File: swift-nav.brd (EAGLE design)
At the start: 53 x 53 mm, 167 parts, among them J1 SMA_EDGE, J6 ZX62-B-5PA, U1 6SLX9FTG256, U10 MAX2769, U12 PT7M8206B33TA5EX, U13 M25PX80, U2 LTC3407A_DFN, U3 STM32-M-64-LQFP, U4 7Q-16.368MBG-T, U5 SMA_PATCH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

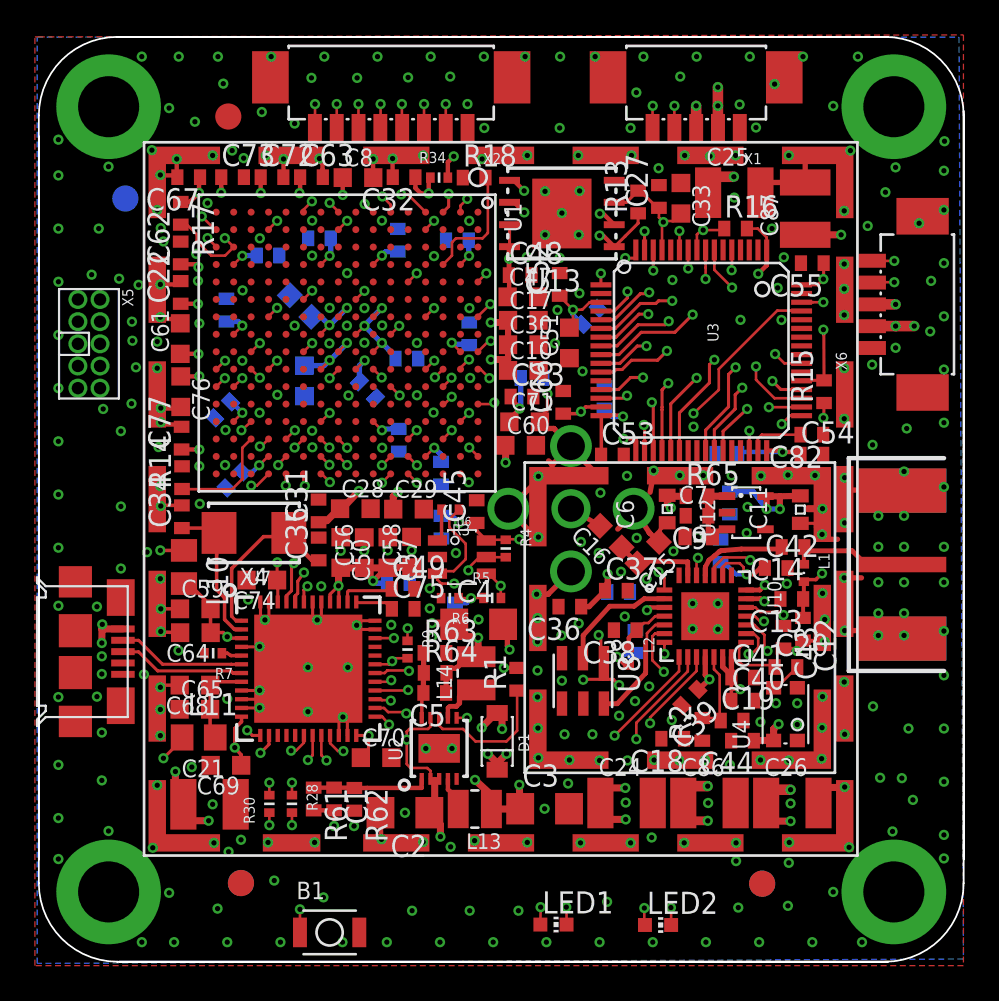
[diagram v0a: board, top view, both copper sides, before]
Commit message: Moved around a few vias and added a few more.
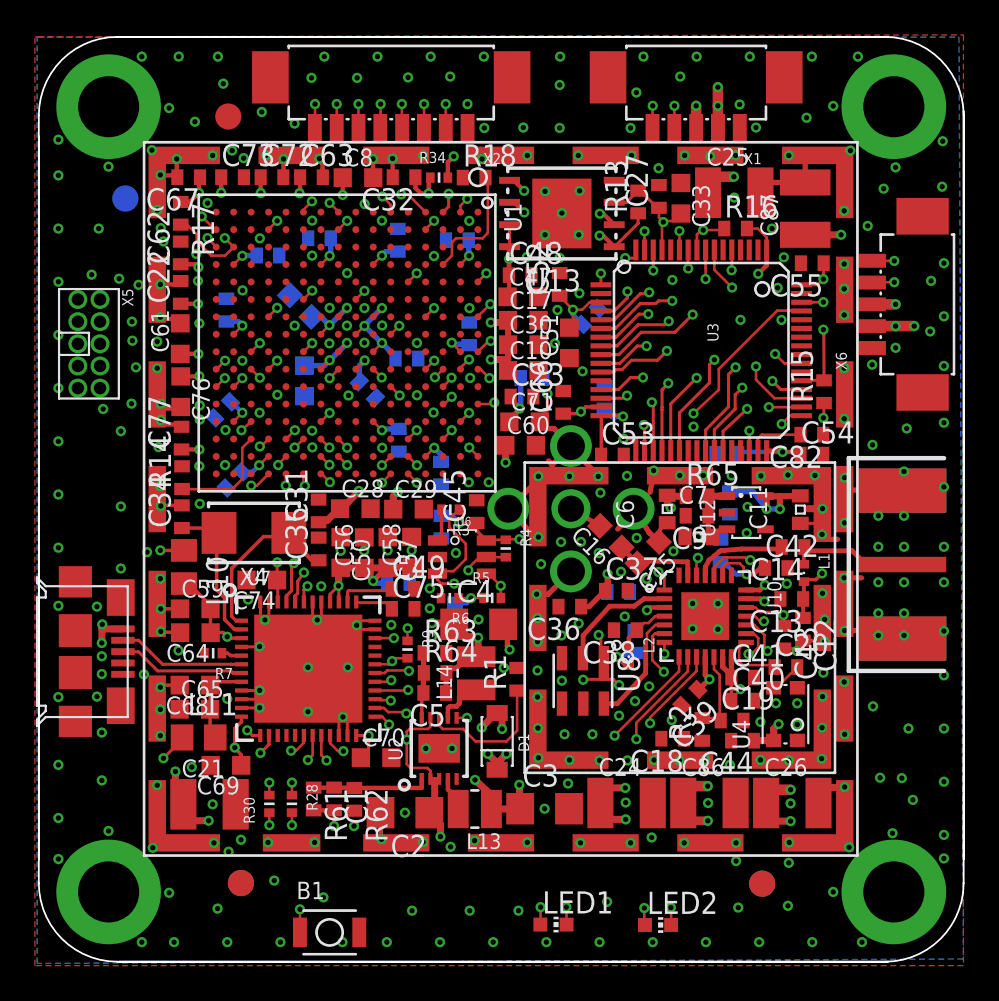
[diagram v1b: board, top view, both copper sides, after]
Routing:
- net JTAG_TDI: track 24.2 -> 25.2 mm
- net JTAG_TDO: track 47.5 -> 48.5 mm
- net MAX_ANT_FLAG: track 92.7 -> 93.3 mm
- net GND: vias 365 -> 370

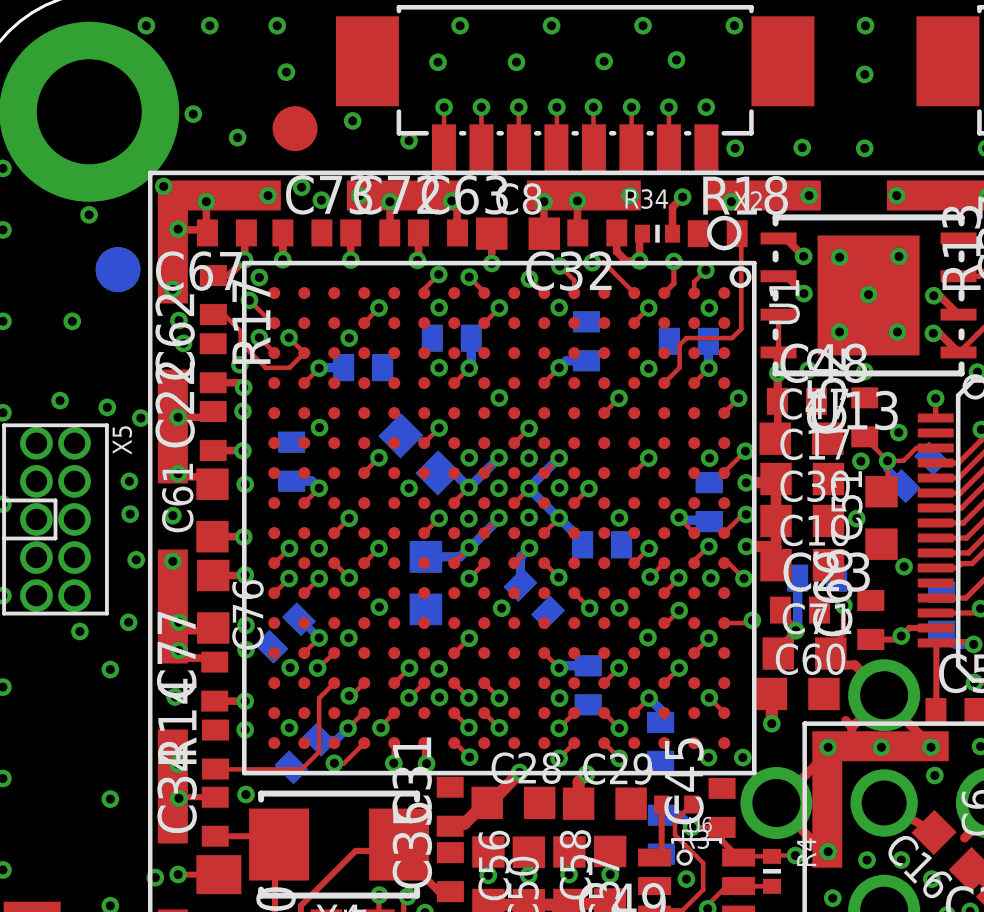
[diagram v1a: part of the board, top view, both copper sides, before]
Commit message: Stuffed in a bunch more vias
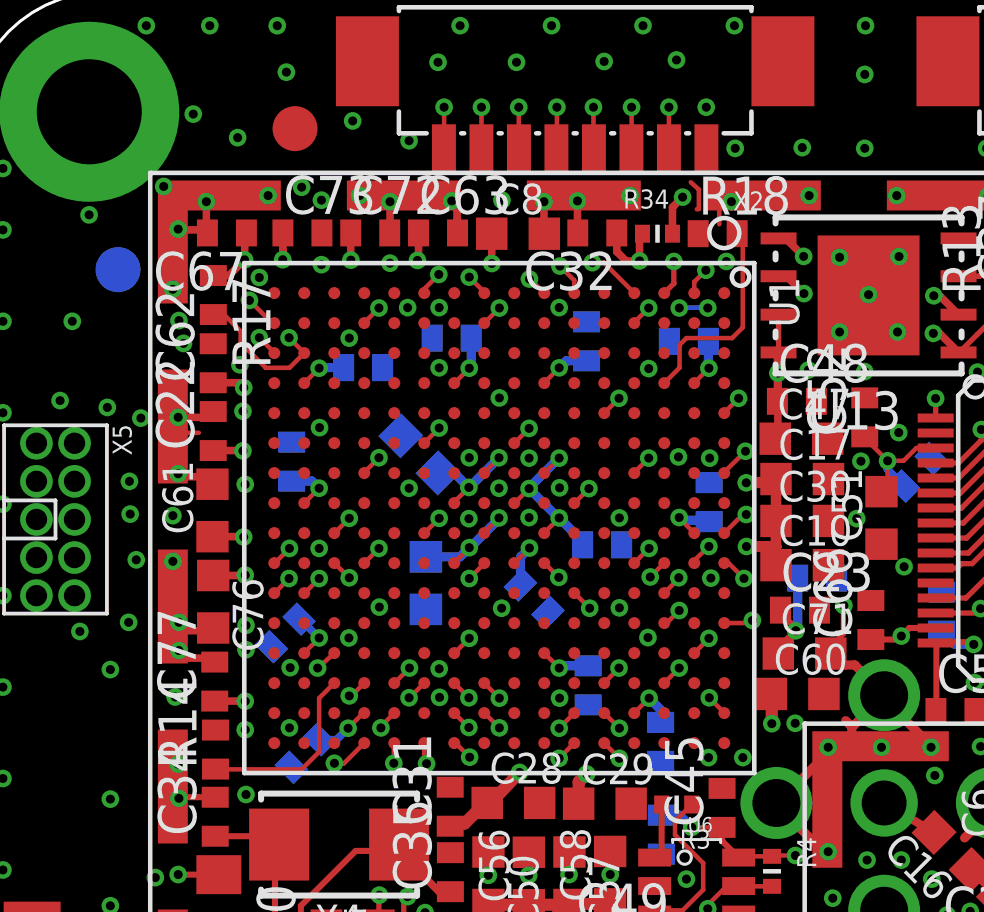
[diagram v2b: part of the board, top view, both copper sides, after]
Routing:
- net GND: track 91.6 -> 94.9 mm, vias 370 -> 378
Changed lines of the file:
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@@
 <setting verticaltext="up"/>
 </settings>
-<grid distance="4" unitdist="mil" unit="mil" style="lines" multiple="1" display="yes" altdistance="0.05" altunitdist="mm" altunit="mm"/>
+<grid distance="0.05" unitdist="mm" unit="mm" style="lines" multiple="1" display="yes" altdistance="0.01" altunitdist="mm" altunit="mm"/>
 <layers>
 <layer number="1" name="Top" color="4" fill="1" visible="yes" active="yes"/>
@@
 <wire x1="23.0632" y1="45.8724" x2="23.0759" y2="45.8724" width="0.1524" layer="16"/>
 <wire x1="28.566" y1="46.3572" x2="28.5645" y2="46.3572" width="0.1524" layer="1"/>
-<via x="28.067" y="45.8597" extent="1-16" drill="0.3"/>
-<wire x1="28.067" y1="45.8597" x2="28.067" y2="45.8851" width="0.1524" layer="16"/>
+<via x="27.067" y="45.8597" extent="1-16" drill="0.3"/>
+<wire x1="27.067" y1="45.8597" x2="28.067" y2="45.8851" width="0.1524" layer="16"/>
 <via x="26.0477" y="43.8404" extent="1-16" drill="0.3"/>
 <via x="21.0693" y="42.8625" extent="1-16" drill="0.3"/>
@@
 <via x="12.6238" y="35.2806" extent="1-16" drill="0.3"/>
 <via x="12.6238" y="34.4678" extent="1-16" drill="0.3"/>
+<via x="27.0397" y="40.8959" extent="1-16" drill="0.3"/>
+<via x="18.0127" y="45.8724" extent="1-16" drill="0.3"/>
+<via x="28.637" y="47.4097" extent="1-16" drill="0.3"/>
+<via x="28.017" y="45.8597" extent="1-16" drill="0.3"/>
+<wire x1="27.65" y1="49.15" x2="27.72" y2="49.16" width="0.1524" layer="1"/>
+<wire x1="27.72" y1="49.16" x2="27.72" y2="49.81" width="0.1524" layer="1"/>
+<wire x1="27.72" y1="49.81" x2="27.45" y2="50.05" width="0.1524" layer="1"/>
+<wire x1="28.4" y1="48.65" x2="28.4" y2="49.35" width="0.1524" layer="1"/>
+<via x="17.4244" y="47.353" extent="1-16" drill="0.3"/>
+<via x="15.1384" y="47.3038" extent="1-16" drill="0.3"/>
+<via x="21.1552" y="49.453" extent="1-16" drill="0.3"/>
+<wire x1="11.05" y1="41.7" x2="10.5" y2="41.7" width="0.1524" layer="1"/>
+<via x="30.9294" y="32.0166" extent="1-16" drill="0.3"/>
 </signal>
 <signal name="N$3">
@@
 <wire x1="26.566" y1="43.3572" x2="26.569" y2="43.3572" width="0.1524" layer="1"/>
 <wire x1="28.9964" y1="48.3362" x2="28.9964" y2="48.0926" width="0.1524" layer="1"/>
-<wire x1="28.9964" y1="48.0926" x2="29.1338" y2="47.9552" width="0.1524" layer="1"/>
-<wire x1="29.1338" y1="47.9552" x2="29.1338" y2="45.1612" width="0.1524" layer="1"/>
-<wire x1="29.1338" y1="45.1612" x2="28.829" y2="44.8564" width="0.1524" layer="1"/>
+<wire x1="28.9964" y1="48.0926" x2="29.1838" y2="47.9552" width="0.1524" layer="1"/>
+<wire x1="29.1838" y1="47.9552" x2="29.1838" y2="45.2112" width="0.1524" layer="1"/>
+<wire x1="29.1838" y1="45.2112" x2="28.829" y2="44.8564" width="0.1524" layer="1"/>
 <wire x1="28.829" y1="44.8564" x2="27.305" y2="44.8564" width="0.1524" layer="1"/>
 <wire x1="27.305" y1="44.8564" x2="27.0764" y2="44.6278" width="0.1524" layer="1"/>
@@
 <wire x1="47.117" y1="40.8686" x2="48.3616" y2="39.624" width="0.1524" layer="15"/>
 <wire x1="12.7381" y1="46.1137" x2="13.5763" y2="46.1137" width="0.1524" layer="15"/>
-<wire x1="13.5763" y1="46.1137" x2="15.7734" y2="48.3108" width="0.1524" layer="15"/>
-<wire x1="15.7734" y1="48.3108" x2="15.7734" y2="50.292" width="0.1524" layer="15"/>
+<wire x1="13.5763" y1="46.1137" x2="14.45" y2="47" width="0.1524" layer="15"/>
+<wire x1="14.45" y1="47" x2="14.45" y2="47.55" width="0.1524" layer="15"/>
+<wire x1="14.45" y1="47.55" x2="15" y2="48.1" width="0.1524" layer="15"/>
+<wire x1="15" y1="48.1" x2="15.3126" y2="48.35" width="0.1524" layer="15"/>
+<wire x1="15.3126" y1="48.35" x2="15.7734" y2="48.8108" width="0.1524" layer="15"/>
+<wire x1="15.7734" y1="48.8108" x2="15.7734" y2="50.292" width="0.1524" layer="15"/>
 <wire x1="15.7734" y1="50.292" x2="18.796" y2="53.3146" width="0.1524" layer="15"/>
 <wire x1="13.566" y1="45.3668" x2="13.485" y2="45.3668" width="0.1524" layer="1"/>

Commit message: Yet more vias.
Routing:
- net VCCIO: track 162.9 -> 164.8 mm
- net GND: vias 378 -> 396
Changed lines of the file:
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@@
 <layer number="13" name="Route13" color="4" fill="5" visible="no" active="no"/>
 <layer number="14" name="Route14" color="1" fill="6" visible="no" active="yes"/>
-<layer number="15" name="Route15" color="4" fill="6" visible="no" active="yes"/>
+<layer number="15" name="Route15" color="4" fill="6" visible="yes" active="yes"/>
 <layer number="16" name="Bottom" color="1" fill="1" visible="no" active="yes"/>
 <layer number="17" name="Pads" color="2" fill="1" visible="yes" active="yes"/>
@@
 <via x="55.2704" y="16.764" extent="1-16" drill="0.3"/>
 <via x="55.2704" y="19.812" extent="1-16" drill="0.3"/>
-<via x="55.2704" y="22.352" extent="1-16" drill="0.3"/>
+<via x="55.2704" y="22.752" extent="1-16" drill="0.3"/>
 <via x="55.2704" y="25.146" extent="1-16" drill="0.3"/>
 <via x="55.2704" y="27.178" extent="1-16" drill="0.3"/>
-<via x="55.2704" y="30.607" extent="1-16" drill="0.3"/>
+<via x="55.2704" y="31.107" extent="1-16" drill="0.3"/>
 <via x="55.2704" y="34.29" extent="1-16" drill="0.3"/>
 <via x="55.2704" y="37.5412" extent="1-16" drill="0.3"/>
@@
 <via x="53.4924" y="12.6746" extent="1-16" drill="0.3"/>
 <via x="53.2384" y="16.764" extent="1-16" drill="0.3"/>
-<via x="51.2064" y="18.034" extent="1-16" drill="0.3"/>
-<via x="52.9844" y="22.098" extent="1-16" drill="0.3"/>
-<via x="51.5112" y="22.098" extent="1-16" drill="0.3"/>
-<via x="52.9844" y="31.496" extent="1-16" drill="0.3"/>
+<via x="51.2564" y="19.134" extent="1-16" drill="0.3"/>
+<via x="52.9844" y="22.798" extent="1-16" drill="0.3"/>
+<via x="51.5112" y="22.748" extent="1-16" drill="0.3"/>
+<via x="53.0344" y="31.346" extent="1-16" drill="0.3"/>
 <via x="49.5554" y="41.9608" extent="1-16" drill="0.3"/>
 <via x="6.8326" y="45.4152" extent="1-16" drill="0.3"/>
@@
 <via x="8.7122" y="35.3822" extent="1-16" drill="0.3"/>
 <via x="6.4262" y="42.7736" extent="1-16" drill="0.3"/>
-<via x="52.9844" y="28.956" extent="1-16" drill="0.3"/>
-<via x="51.5112" y="28.956" extent="1-16" drill="0.3"/>
-<via x="52.9844" y="23.368" extent="1-16" drill="0.3"/>
-<via x="51.5112" y="23.368" extent="1-16" drill="0.3"/>
+<via x="52.9844" y="28.506" extent="1-16" drill="0.3"/>
+<via x="51.5112" y="28.506" extent="1-16" drill="0.3"/>
+<via x="52.9844" y="23.868" extent="1-16" drill="0.3"/>
+<via x="51.5112" y="23.868" extent="1-16" drill="0.3"/>
 <contactref element="H1" pad="B3,0"/>
 <contactref element="H2" pad="B3,0"/>
@@
 <wire x1="11.05" y1="41.7" x2="10.5" y2="41.7" width="0.1524" layer="1"/>
 <via x="30.9294" y="32.0166" extent="1-16" drill="0.3"/>
+<via x="40.61034375" y="41.36880625" extent="1-16" drill="0.3"/>
+<via x="41.81034375" y="41.31880625" extent="1-16" drill="0.3"/>
+<via x="43.9118" y="38.1328" extent="1-16" drill="0.3"/>
+<via x="55.3204" y="28.478" extent="1-16" drill="0.3"/>
+<via x="55.2704" y="23.878" extent="1-16" drill="0.3"/>
+<via x="52.9844" y="19.948" extent="1-16" drill="0.3"/>
+<via x="53.0344" y="18.348" extent="1-16" drill="0.3"/>
+<via x="55.2844" y="18.348" extent="1-16" drill="0.3"/>
+<via x="51.0344" y="17.848" extent="1-16" drill="0.3"/>
+<via x="51.0344" y="16.648" extent="1-16" drill="0.3"/>
+<via x="55.2704" y="32.807" extent="1-16" drill="0.3"/>
+<via x="52.8204" y="32.357" extent="1-16" drill="0.3"/>
+<via x="50.9844" y="30.096" extent="1-16" drill="0.3"/>
+<via x="55.2704" y="29.757" extent="1-16" drill="0.3"/>
+<via x="52.9704" y="29.607" extent="1-16" drill="0.3"/>
+<via x="55.2704" y="21.202" extent="1-16" drill="0.3"/>
+<via x="53.0344" y="21.248" extent="1-16" drill="0.3"/>
+<via x="51.4844" y="21.098" extent="1-16" drill="0.3"/>
 </signal>
 <signal name="N$3">
@@
 <vertex x="56.3626" y="3.5052"/>
 <vertex x="56.3626" y="13.9192"/>
-<vertex x="56.388" y="32.004"/>
-<vertex x="49.022" y="32.004"/>
+<vertex x="56.338" y="32.204"/>
+<vertex x="53.45" y="32.2"/>
+<vertex x="53.4" y="32.2"/>
+<vertex x="53.05" y="31.85"/>
+<vertex x="52.6" y="31.85"/>
+<vertex x="52.296" y="32.204"/>
+<vertex x="49.172" y="32.204"/>
 <vertex x="49.0728" y="31.9532"/>
 <vertex x="49.0728" y="13.9192"/>
@@
 <wire x1="17.907" y1="12.946" x2="17.907" y2="13.6652" width="0.1524" layer="1"/>
 <via x="17.907" y="13.6652" extent="1-16" drill="0.3"/>
-<wire x1="49.3014" y1="32.1691" x2="52.082290625" y2="32.16329375" width="0.4064" layer="3"/>
-<wire x1="52.082290625" y1="32.16329375" x2="55.3847" y2="32.1564" width="0.4064" layer="3"/>
+<wire x1="49.3014" y1="32.1691" x2="51.832290625" y2="31.31329375" width="0.4064" layer="3"/>
+<wire x1="51.832290625" y1="31.31329375" x2="52.55" y2="30.5" width="0.4064" layer="3"/>
+<wire x1="52.55" y1="30.5" x2="53.7283" y2="30.5" width="0.4064" layer="3"/>
+<wire x1="53.7283" y1="30.5" x2="55.3847" y2="32.1564" width="0.4064" layer="3"/>
 <wire x1="27.4828" y1="28.5496" x2="28.0162" y2="28.9306" width="0.4064" layer="3"/>
 <wire x1="28.0162" y1="28.9306" x2="28.6258" y2="29.3116" width="0.6096" layer="3"/>
@@
 <wire x1="51.4731" y1="33.782" x2="51.8922" y2="33.3629" width="0.4064" layer="3"/>
 <wire x1="51.8922" y1="33.3629" x2="51.8922" y2="32.353384375" width="0.4064" layer="3"/>
-<wire x1="51.8922" y1="32.353384375" x2="52.082290625" y2="32.16329375" width="0.4064" layer="3"/>
+<wire x1="51.8922" y1="32.353384375" x2="51.832290625" y2="31.31329375" width="0.4064" layer="3"/>
 <wire x1="26.8398" y1="49.2172" x2="27.178" y2="49.5554" width="0.254" layer="1"/>
 <wire x1="20.32" y1="12.0754" x2="20.32" y2="11.176" width="0.2032" layer="1"/>
